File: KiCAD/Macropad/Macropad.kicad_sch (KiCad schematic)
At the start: 29 parts, among them SW1 SW_Push_45deg, SW2 SW_Push_45deg, SW3 SW_Push_45deg, SW4 SW_Push_45deg, SW5 SW_Push_45deg, SW6 SW_Push_45deg, SW7 EC1110120201, U1 XIAO-RP2040-DIP, U2 SSD1306

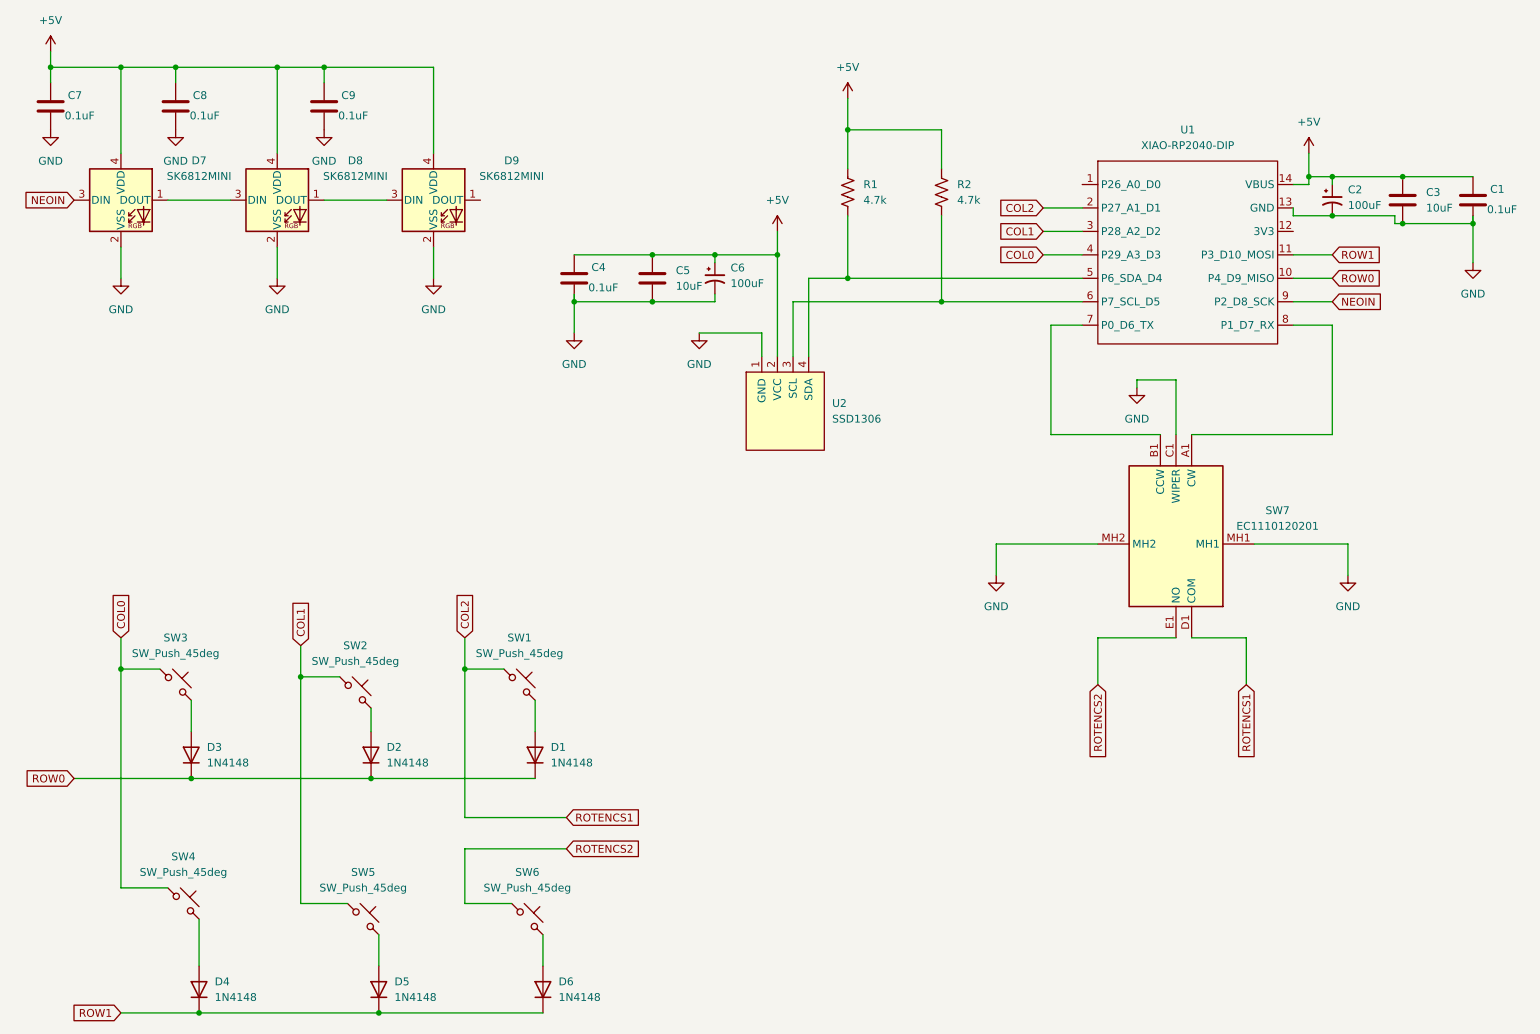
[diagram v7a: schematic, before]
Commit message: Updated schematic and layout with new EC11 rotary encoder.
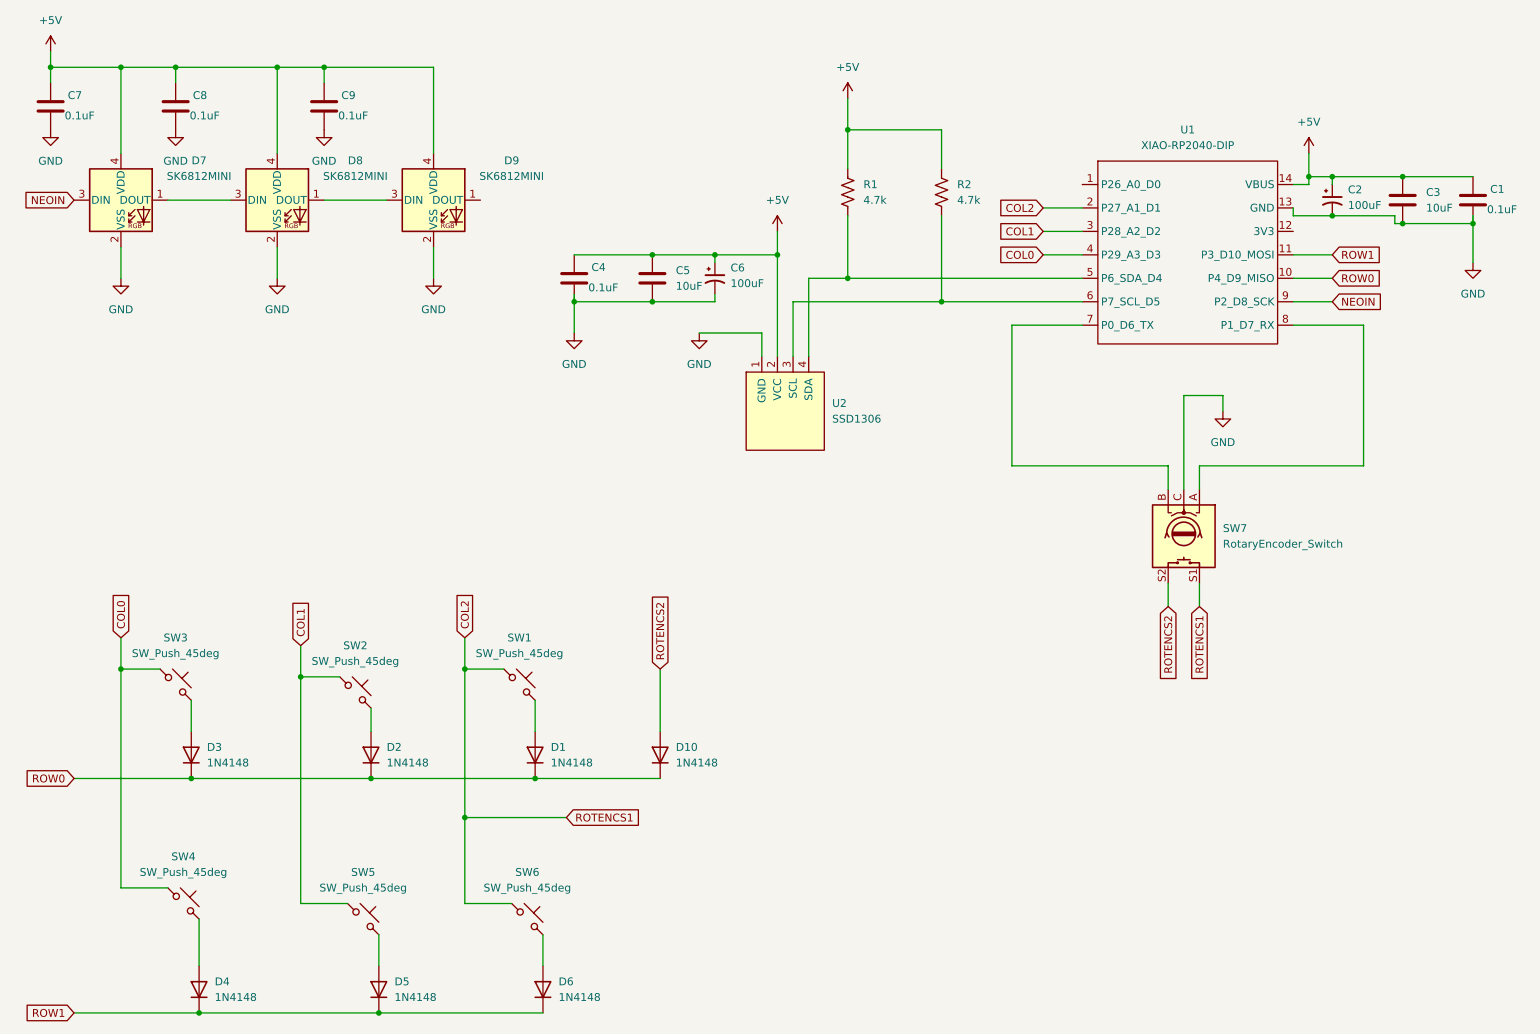
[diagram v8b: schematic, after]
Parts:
- removed SW7: EC1110120201, EC1110120201_Rotary_Encoder:EC1110120201, symbol EC1110120201:EC1110120201
- added D10: 1N4148, Diode_THT:D_DO-35_SOD27_P7.62mm_Horizontal, symbol Diode:1N4148
- added SW7: RotaryEncoder_Switch, Rotary_Encoder:RotaryEncoder_Alps_EC11E-Switch_Vertical_H20mm, symbol Device:RotaryEncoder_Switch
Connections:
- net COL2: now also SW6.1, SW7.S1
- net GND: now also SW7.C
- net ROTENCS2: now also D10.2 (A), SW7.S2; no longer SW6.1
- net ROW0: now also D10.1 (K)
- net at U1.8 (P1_D7_RX): now also SW7.A
- net at U1.7 (P0_D6_TX): now also SW7.B
